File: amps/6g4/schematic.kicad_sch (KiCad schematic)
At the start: 77 parts, among them T1 8087, T2 45216

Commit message: Fix: schematic sheets — real title block, fitted paper, no lettering through circuitry
Every sheet in the corpus shipped with an EMPTY title block ("Title:" and
"Date:" blank, default "Sheet /" furniture) laid onto a fixed A4/A3 page
regardless of the drawing's size, with prose annotations placed by hand
wherever a coordinate looked free when the amp was first drawn. The result
read as an unfinished alpha under a `verified` badge: KiCanvas's default view
is `zoom_to_page()`, so a 150 x 110 mm circuit on an A3 sheet opened as a
postage stamp, and later edits had pushed live circuitry under the prose.

schematic_lib.py — the builder now records each element as a (kind, points,
extra) tuple instead of a finished string, so `write()` can measure and move
what it emits:

- emits a real `(title_block …)` read from the amp's own meta.yaml — Title =
  designation + style, Date = the verification (or added) date, Rev = the
  verification status, Company = Circuit Codex, plus the licence and source
  URL as comments. Fixes all 34 sheets from one place;
- emits `(paper "User" w h)` cut to the drawing, translated to a fixed margin,
  with the bottom 34 mm strip reserved for the worksheet's title block. Sheet
  utilisation of the drawable area went from as low as ~20% to 92-98%;
- `note()` queues prose into a wrapped band under the circuit, and `caption()`
  places a section heading over the block it names, nudging it clear if it
  would print through anything;
- per-symbol default label offsets (the old single default printed every pot's
  value through its own wiper arrow and every transformer's designator through
  its body), plus `place_labels()`, which moves any designator/value block that
  would print over ink;
- transformers and chokes are drawn, not boxed: iron core between two windings,
  centre taps where the part has them, and an optional `spec` lettering slot for
  a ratio or impedance;
- `gnd()` takes a direction, because a flag defaulting to "down" at the HEAD of
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
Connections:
- net BP1: no longer CTO1.1, RINT.2, RTO1.2, V2B.1 (P)
- net GND: no longer CTOFB.2, RTOFB.1, V2B.2 (G)
- new net: CTOFB.2, RTOFB.1, V2B.2 (G)
- new net: CTO1.1, RINT.2, RTO1.2, V2B.1 (P)
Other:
- note added: "Long-tailed-pair phase inverter (V5)"
- note added: "The phase inverter runs off the BC rail — BP1 through the drawing's own 10k dropper, RD1."
- note removed: "6G4 — Brown Super-style · Circuit Codex · CC-BY-SA 4.0 · redrawn from circuit facts"
- note removed: "Long-tailed-pair phase inverter (V5) — off the BC rail (BP1 via the drawing's own 10k dropper, RD1)"
- company: (none) -> Circuit Codex
- title: (none) -> 6G4 — Brown Super-style

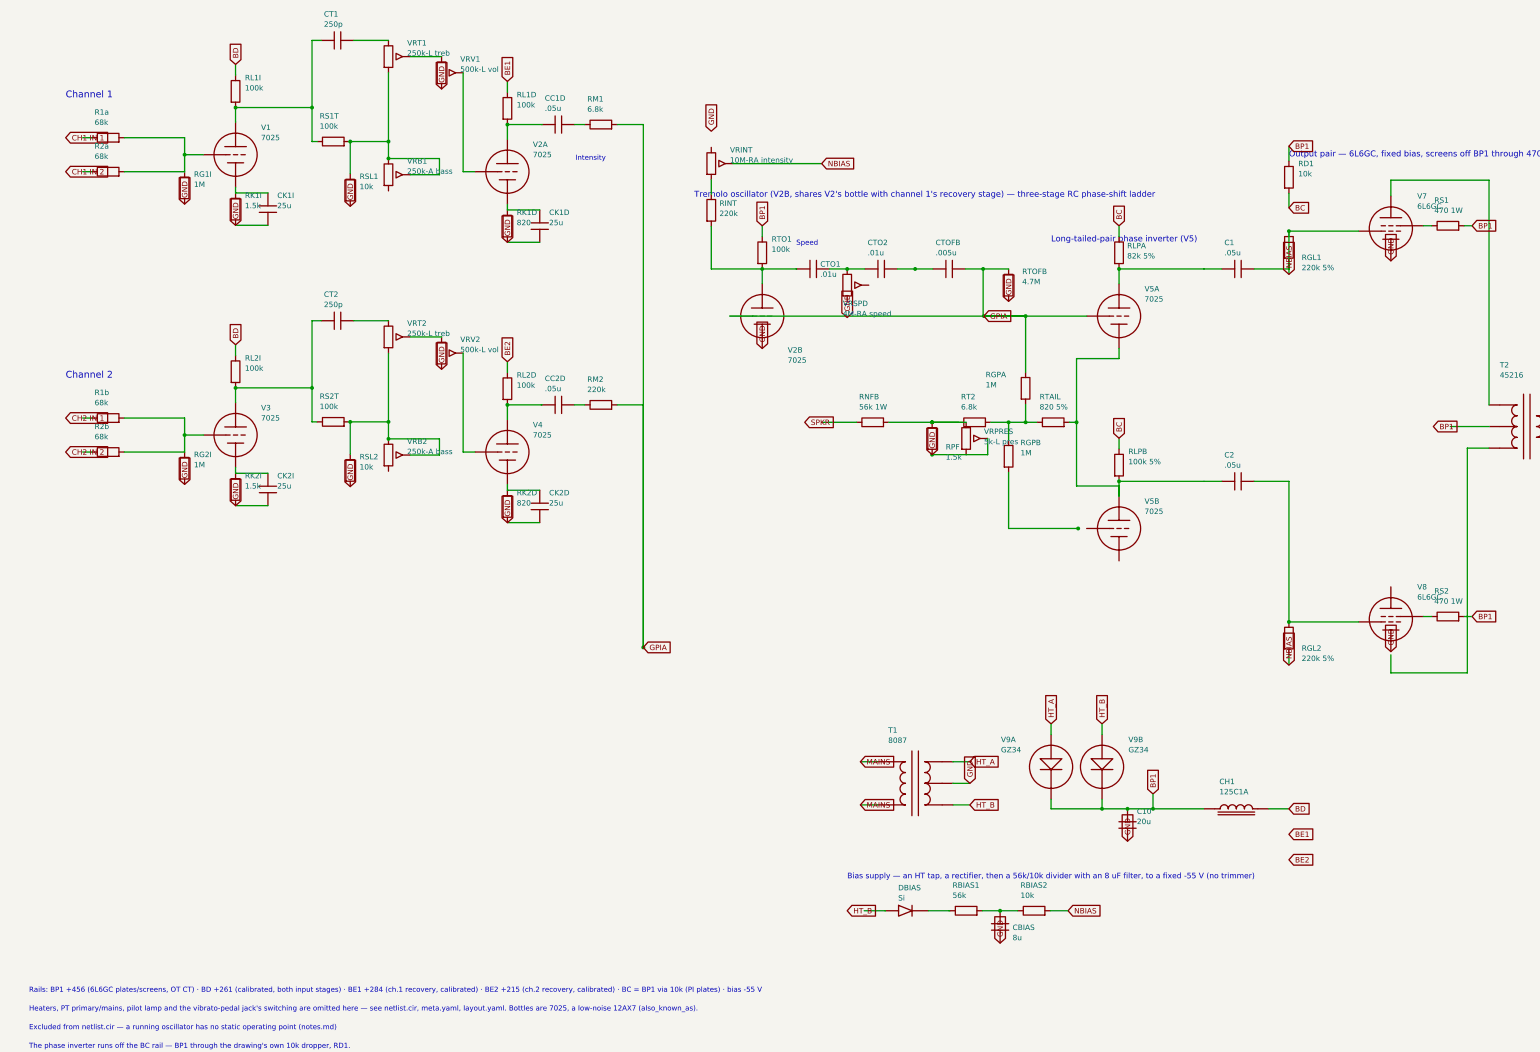
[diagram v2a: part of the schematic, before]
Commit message: Fix: label-wire abutments the gate cannot see, caught by reading pixels
Four sites from the closing visual pass, each a designator or value line
sitting on live wiring below gate sensitivity (wires are not a clash class,
and the old placement ruler under-read text width):

- 5F6-A: RB2's block, squeezed into the 2.5 mm channel beside C15, printed
  through its own resistor body and into C15b's designator. Authored anchor
  now letters it above the supply wire, between RB1's lettering and the -48V
  flag — the one clear pocket in that cramped bias block.
- 6G4: the Speed pot's "4M-RA speed" value line lay on the oscillator ladder
  wire and CTO2's pin; anchored clear (the true-ruler placer settles it left
  of the pot).
- 6G5: RNFB's vertical lettering straddled the NFB wire itself. Drawn
  directly instead of via series_h so the block can be pinned horizontal
  under the part. Also: the tremolo caption was a 175 mm single-sentence
  banner — wider than any clear band on the sheet, printing across the bias
  diodes wherever it was placed. It keeps its headline beside the V3 bottle;
  the mechanism sentence is a note, and notes live in the band.
- 1959: both volume pots' "1M vol" crossed the wiper wire and RM1/RM2's
  pins; anchored clear of the pot body (placer settles them left).

6G6-B's RK2B/CK2B crowding (the fourth verdict item) needed no draw-script
change: the renderer-metric placer from the previous commit already moves the
block clear of the tie wire.

🤖 Generated with [Claude Code](https://claude.com/claude-code)

Co-Authored-By: Claude Fable 5 <noreply@anthropic.com>
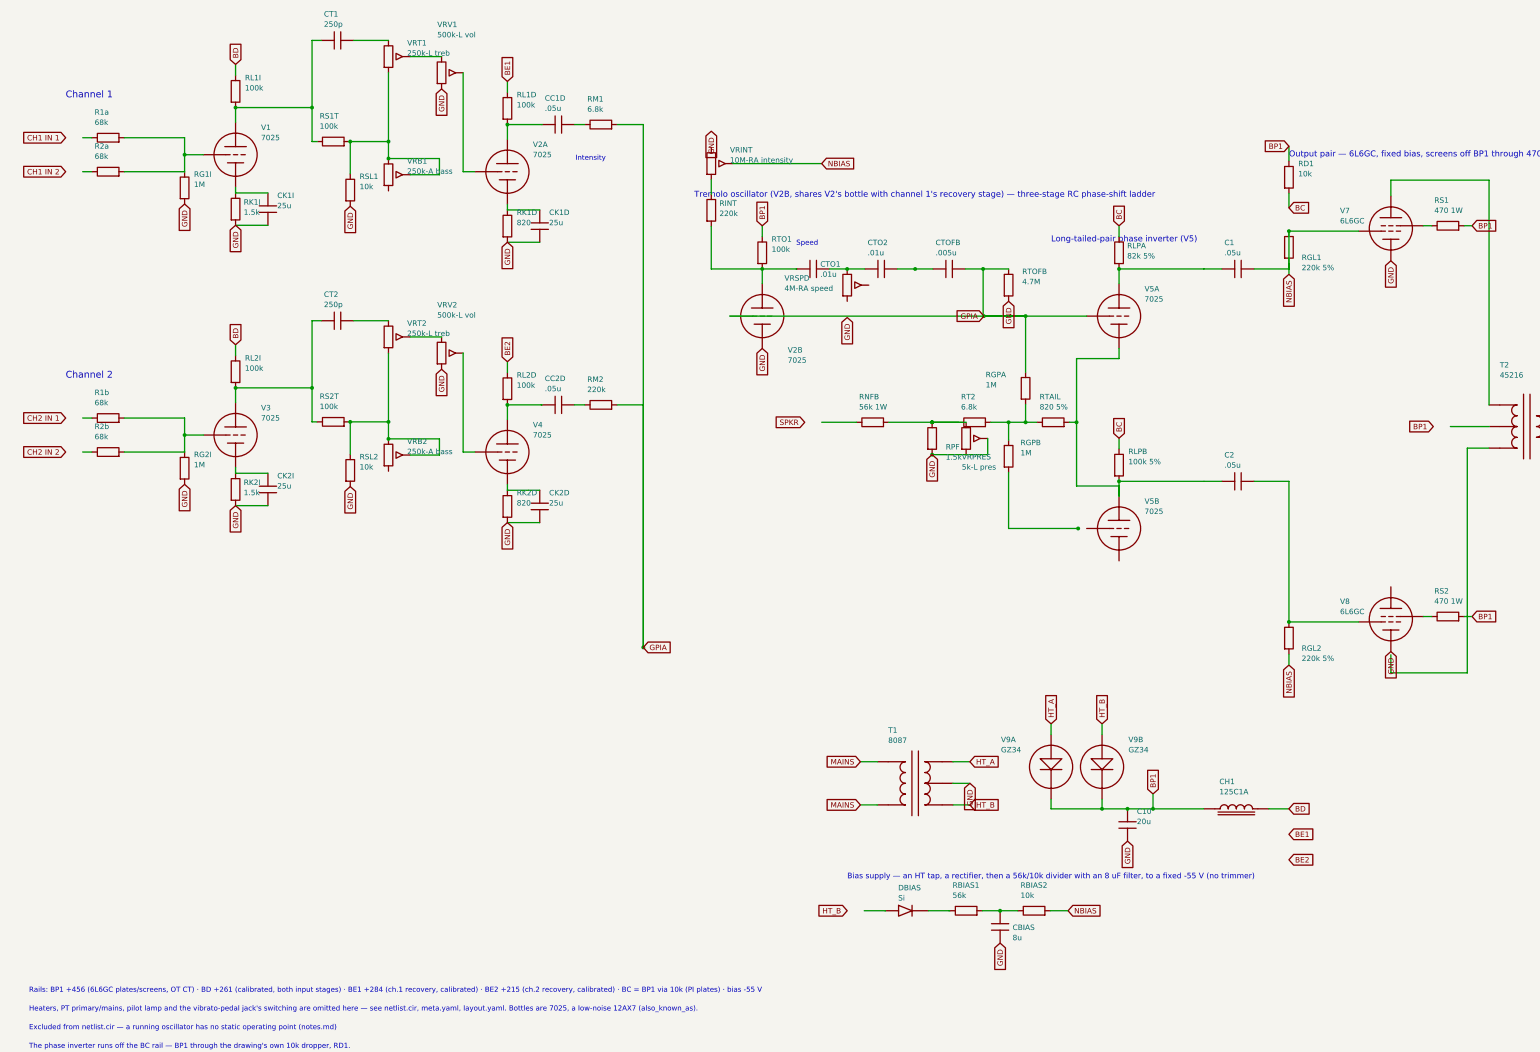
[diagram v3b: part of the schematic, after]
